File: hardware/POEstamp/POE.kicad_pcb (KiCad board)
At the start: 4 copper layers, 100 x 50 mm, 127 parts, among them J1 0813-1X1T-57-F, J2 SWD, J3 MCU Port B, J4 MCU Port C, P1 PoE-, P2 PoE+, P3 GND, P4 +5V, P5 +12V, P6 +3V3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

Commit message: Included BOM info on everything except transistors. Updated many footprints to IPC footprints. Also added a SOD-128 footprint.
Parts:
- removed 1PIN (x4): P***, Connect:1pin
- removed C1: 0.1uF, 100V, X7R, Capacitors_SMD:c_0805
- removed C10, C11: 10nF, Capacitors_SMD:c_0603
- removed C12, C31, C37: 1uF, Capacitors_SMD:c_0603
- removed C13: 33nF, Capacitors_SMD:c_0603
- removed C14, C15: 100uF, 6.3V, X5R, Capacitors_SMD:c_1206
- removed C16, C18: 10uF, Capacitors_SMD:c_1206
- removed C17, C22, C24, C25: 10uF, Capacitors_SMD:c_0805
- removed C19, C26, C27, C28, C29, C30, C32, C33, C34, C35, C36, C38, C39: 100nF, Capacitors_SMD:c_0603
- removed C2: 1uF, 100V, Capacitors_SMD:c_1206
- removed C20: 47nF, Capacitors_SMD:c_0805
- removed C21: 180nF, Capacitors_SMD:c_0805
- removed C23: 22uF, Capacitors_SMD:c_0805
- removed C3: 68pF, 200V, Capacitors_SMD:c_0603
- removed C4: 4.7uF, 10V, Capacitors_SMD:c_0805
- removed C5: 4.7uF, 100v, rfid:EEE-2AA4R7UP
- removed C6: 470pF, Capacitors_SMD:c_0603
- removed C7: 27nF, Capacitors_SMD:c_0805
- removed C8: 2.8nF, 250VAC, YCAP, rfid:kemet_C900
- removed C9: 220uF, 6.3v, rfid:EEE-FK0J221P
- removed D1: SMB540, SMD_Packages:DO-214-AA_SMB
- removed D10, D11: LED, LEDs:LED-0603
- removed D12: 5V LED, LEDs:LED-0603
- removed D13: 1N5189, rfid:SOD-123
- removed D14: 1N4148, rfid:SOD-123
- removed D15: MBRA340T3G, SMD_Packages:DO-214-AC_SMA
- removed D16: 12V LED, LEDs:LED-0603
- removed D17: 3V3 LED, LEDs:LED-0603
- removed D2: SMAJ58A, SMD_Packages:DO-214-AC_SMA
- removed D3, D4, D7: BAS516, rfid:SOD-523
- removed D5: 1N5237B, 8.2V, rfid:SOD-123
- removed D6, D9: CDNBS04-B08200, rfid:CDNBS04
- removed D8: TLV431, SMD_Packages:SOT-23
- removed G1: 25MHz OSC, rfid:Si501_2.5x2
- removed G2: 24MHz OSC, rfid:Si501_2.5x2
- removed J1: 0813-1X1T-57-F, rfid:0813-1X1T-57-F
- removed J2: SWD, rfid:JST_PH_5pin
- removed J3: MCU Port B, rfid:16_pin_breakout
- removed J4: MCU Port C, rfid:16_pin_breakout
- removed L1: 3.3uH, SMD_Packages:SMD-0805
- removed L2: choke, SMD_Packages:SMD-0805
- removed L3: 10uH, rfid:SRU1048
- removed L4: 15uH, rfid:NR6028
- removed P1: PoE-, Connect:PINTST
- removed P2: PoE+, Connect:PINTST
- removed P3: GND, Connect:PINTST
- removed P4: +5V, Connect:PINTST
- removed P5: +12V, Connect:PINTST
- removed P6: +3V3, Connect:PINTST
- removed P7: 12V_Switch, rfid:SIL2-3.5mm
- removed Q1: SI3440DV, NFET, rfid:TSOP-6
- removed Q2: MMBTA42, SMD_Packages:SOT-23_Inv2
- removed Q3: 2N7002, SMD_Packages:SOT-23-GDS
- removed Q4: MOSFET_N, SMD_Packages:SOT-23-GDS
- removed R1, R26, R29, R36: 10k, SMD_Packages:SMD-0603
- removed R10: 10R, SMD_Packages:SMD-0603
- removed R11, R17, R20: 1k, SMD_Packages:SMD-0603
- removed R12: 47k, SMD_Packages:SMD-0603
- removed R13: 100k, 1%, SMD_Packages:SMD-0603
- removed R14: 33.2k, SMD_Packages:SMD-0603
- removed R15, R16, R18, R19: 49R9, SMD_Packages:SMD-0603
- removed R2, R3: 220K, SMD_Packages:SMD-0603
- removed R21, R35: 470R, SMD_Packages:SMD-0603
- removed R22, R30: 2.8k, SMD_Packages:SMD-0603
- removed R23: 226k, SMD_Packages:SMD-0603
- removed R24: 1.4k, SMD_Packages:SMD-0805
- removed R25: 31.2k, SMD_Packages:SMD-0603
- removed R27: 143k, SMD_Packages:SMD-0603
- removed R28: 16.2k, SMD_Packages:SMD-0603
- removed R31: 2.32k, SMD_Packages:SMD-0603
- removed R32, R33: 24.9, SMD_Packages:SMD-0603
- removed R34: 4.7k, SMD_Packages:SMD-0603
- removed R4, R400: 0.250R, SMD_Packages:SMD-0805
- removed R5: 4.7K, SMD_Packages:SMD-0603
- removed R6: 510R, SMD_Packages:SMD-0603
- removed R7: 100R, 1/8W, SMD_Packages:SMD-0805
- removed R8: 100k, SMD_Packages:SMD-0603
- removed R9: 6.8k, SMD_Packages:SMD-0603
- removed SW1: reset, rfid:TE-Switch-FSM-JSM
- removed SYM: Symbol_OSHW-Logo_SilkScreen_07Jul2012, Symbols:Symbol_OSHW-Logo_SilkScreen
- removed T1: PA1134, rfid:PA1134
- removed U1: LTC4267-3, rfid:SSOP-16
- removed U2: ENC28J60, SMD_Packages:SSOP-28
- removed U3: PS2811, rfid:SSOP-4
- removed U4: MCP16301, SMD_Packages:SOT-23-6
- removed U5: TPS61175, rfid:HTSSOP-14-1EP
- removed U6: STM32F100RC, rfid:LQFP64
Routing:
- net 3V3: track 196.8 -> 0.00 mm, vias 11 -> 0
- net GND: track 172.3 -> 0.00 mm, vias 62 -> 0
- net 5VPoE: track 123.2 -> 0.00 mm, vias 16 -> 0
- net /EthernetINT: track 88.5 -> 0.00 mm, vias 2 -> 0
- net /EthernetSI: track 85.5 -> 0.00 mm, vias 2 -> 0
- net /EthernetSO: track 85.1 -> 0.00 mm, vias 2 -> 0
- net /EthernetSCK: track 84.6 -> 0.00 mm, vias 2 -> 0
- net /EthernetCS: track 84.3 -> 0.00 mm, vias 2 -> 0
- net GNDA: track 68.3 -> 0.00 mm, vias 14 -> 0
- net /nRST: track 54.5 -> 0.00 mm
- net /PVcc: track 42.1 -> 0.00 mm, vias 3 -> 0
- net /PB15: track 37.4 -> 0.00 mm, vias 1 -> 0
- net Net-(C2-Pad1): track 34.4 -> 0.00 mm, vias 1 -> 0
- net /PB10: track 34.4 -> 0.00 mm, vias 1 -> 0
- net /12VSwitch: track 33.1 -> 0.00 mm, vias 2 -> 0
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- removed copper zone on F.Cu, net 12V
- removed copper zone on In1.Cu, net 12V
- removed copper zone on B.Cu, net 3V3
- removed copper zone on F.Cu, net 3V3
- removed copper zone on B.Cu, net 5VPoE
- removed copper zone on F.Cu, net 5VPoE
- removed copper zone on B.Cu, net GND
- removed copper zone on F.Cu, net GND
- removed copper zone on In2.Cu, net GND
- removed copper zone on B.Cu, net GNDA
- removed copper zone on F.Cu, net GNDA
- removed copper zone on In2.Cu, net GNDA
- removed copper zone on F.Cu, net Net-(C19-Pad2)
- removed copper zone on F.Cu, net Net-(D1-Pad1)
- removed copper zone on F.Cu, net Net-(D15-Pad1)
- removed copper zone on B.Cu, net Net-(Q1-Pad1)
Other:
- board outline removed
- board text removed: "+"
- board text removed: "-"
- board text removed: "1"
- board text removed: "12V"
- board text removed: "2"
- board text removed: "3"
- board text removed: "3.3V"
- board text removed: "4"
- board text removed: "5V"
- board text removed: "Board Layers:"
- board text removed: "CERN OHL v1.2"
- board text removed: "GND"
- board text removed: "Jon Neal https://github.com/reportingsjr/rfidBoard Version 1"
- board text removed: "MCU Port B"
- board text removed: "MCU Port C"
- board text removed: "Pin 1"
- board text removed: "Reset"

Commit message: Initial netlist import and layer setup.
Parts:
- added C1: 0.1uF, 100V, X7R, IPC7351-Nominal:CAPC2012X95, F.Cu at (188.6, 111.5)
- added C10: 100nF, IPC7351-Nominal:CAPC1608X90, F.Cu at (191.1, 123.3)
- added C11: 100nF, IPC7351-Nominal:CAPC1608X90, F.Cu at (205.3, 110.6)
- added C12: 1uF, IPC7351-Nominal:CAPC1608X90, F.Cu at (206.4, 114.5)
- added C13: 33nF, IPC7351-Nominal:CAPC1608X95, F.Cu at (198.9, 121.8)
- added C14: 100uF, 6.3V, X5R, IPC7351-Nominal:CAPC3216X180, F.Cu at (194.9, 105.8)
- added C15: 100uF, 6.3V, X5R, IPC7351-Nominal:CAPC3216X180, F.Cu at (201.8, 96.3)
- added C16: 1uF, IPC7351-Nominal:CAPC1608X90, F.Cu at (213.6, 106.1)
- added C17: 1uF, IPC7351-Nominal:CAPC1608X90, F.Cu at (217.5, 103.6)
- added C2: 1uF, 100V, IPC7351-Nominal:CAPC3216X180, F.Cu at (217.3, 89.1)
- added C3: 68pF, 200V, IPC7351-Nominal:CAPC1608X87, F.Cu at (171.9, 123.6)
- added C4: 4.7uF, 10V, IPC7351-Nominal:CAPC2012X135, F.Cu at (217.5, 86.5)
- added C5: 4.7uF, 100v, rfid:EEE-2AA4R7UP, F.Cu at (174.5, 117.4)
- added C6: 470pF, IPC7351-Nominal:CAPC1608X90, F.Cu at (191.1, 121.3)
- added C7: 27nF, IPC7351-Nominal:CAPC2012X88, F.Cu at (209.9, 109.3)
- added C8: 2.8nF, 250VAC, YCAP, IPC7351-Nominal:CAPC4532X150, F.Cu at (189.7, 96.2)
- added C9: 220uF, 6.3v, rfid:EEE-FK0J221P, F.Cu at (151.8, 120.2)
- added D1: PMEG3050EP, rfid:SOD-128, F.Cu at (206.2, 101.8)
- added D12: 5V LED, LEDs:LED-0603, F.Cu at (214.1, 98.2)
- added D2: SMAJ58A, IPC7351-Nominal:DIOM5436X265, F.Cu at (164.4, 121.8)
- added D3: BAS516, rfid:SOD-523, F.Cu at (192.0, 115.3)
- added D4: BAS516, rfid:SOD-523, F.Cu at (200.2, 109.8)
- added D5: 1N5237B, 8.2V, rfid:SOD-123, F.Cu at (194.8, 101.5)
- added D6: CDNBS04-B08200, rfid:CDNBS04, F.Cu at (189.3, 88.3)
- added D7: BAS516, rfid:SOD-523, F.Cu at (217.1, 93.0)
- added D8: TLV431, smd-semi:SOT-23, F.Cu at (205.6, 107.7)
- added D9: CDNBS04-B08200, rfid:CDNBS04, F.Cu at (175.7, 104.3)
- added J1: 0813-1X1T-57-F, rfid:0813-1X1T-57-F, F.Cu at (152.5, 92.5)
- added L1: 3.3uH, IPC7351-Nominal:INDC2012X130, F.Cu at (209.9, 106.9)
- added P1: PoE-, Connect:PINTST, F.Cu at (202.4, 114.7)
- added P2: PoE+, Connect:PINTST, F.Cu at (213.5, 103.0)
- added P3: GND, Connect:PINTST, F.Cu at (195.4, 120.3)
- added P4: +5V, Connect:PINTST, F.Cu at (218.7, 98.0)
- added P5: CONN_01X05, conn-2mm:CONN-2MM-F-1x5, F.Cu at (214.8, 83.1)
- added P6: 5Vout, Connect:1pin, F.Cu at (211.5, 89.5)
- added P7: GNDout, Connect:1pin, F.Cu at (186.0, 116.9)
- added Q1: SI3440DV, NFET, rfid:TSOP-6, F.Cu at (202.2, 88.0)
- added Q2: 2N7002, smd-semi:SOT-23, F.Cu at (197.6, 114.4)
- added Q3: MMBTA42, smd-semi:SOT-23, F.Cu at (186.0, 122.5)
- added R1: 10k, IPC7351-Nominal:RESC1608X55, F.Cu at (221.0, 101.1)
- added R10: 10R, IPC7351-Nominal:RESC1608X55, F.Cu at (209.9, 111.5)
- added R11: 1k, IPC7351-Nominal:RESC1608X55, F.Cu at (206.4, 116.5)
- added R12: 47k, IPC7351-Nominal:RESC1608X55, F.Cu at (209.9, 114.5)
- added R13: 100k, 1%, IPC7351-Nominal:RESC1608X55, F.Cu at (178.6, 123.6)
- added R14: 33.2k, IPC7351-Nominal:RESC1608X55, F.Cu at (199.0, 117.9)
- added R2: 220K, IPC7351-Nominal:RESC1608X55, F.Cu at (194.9, 123.4)
- added R21: 470R, IPC7351-Nominal:RESC1608X55, F.Cu at (206.4, 112.6)
- added R22: 2.8k, IPC7351-Nominal:RESC1608X55, F.Cu at (217.0, 106.1)
- added R3: 220K, IPC7351-Nominal:RESC1608X55, F.Cu at (217.5, 101.6)
- added R4: 0.250R, IPC7351-Nominal:RESC2013X65, F.Cu at (211.4, 94.4)
- added R400: 0.250R, IPC7351-Nominal:RESC2013X65, F.Cu at (191.3, 119.1)
- added R5: 4.7K, IPC7351-Nominal:RESC1608X55, F.Cu at (202.4, 119.8)
- added R6: 510R, IPC7351-Nominal:RESC1608X55, F.Cu at (198.9, 119.8)
- added R7: 100R, 1/8W, IPC7351-Nominal:RESC2012X70, F.Cu at (193.2, 108.4)
- added R8: 100k, IPC7351-Nominal:RESC1608X55, F.Cu at (202.6, 117.9)
- added R9: 6.8k, IPC7351-Nominal:RESC1608X55, F.Cu at (213.5, 109.1)
- added T1: PA1134, rfid:PA1134, F.Cu at (171.8, 95.9)
- added U1: LTC4267-3, IPC7351-Nominal:SOP63P600X175-16, F.Cu at (164.3, 116.3)
- added U3: PS2811, rfid:SSOP-4, F.Cu at (186.0, 104.3)
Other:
- copper layers 4 -> 2

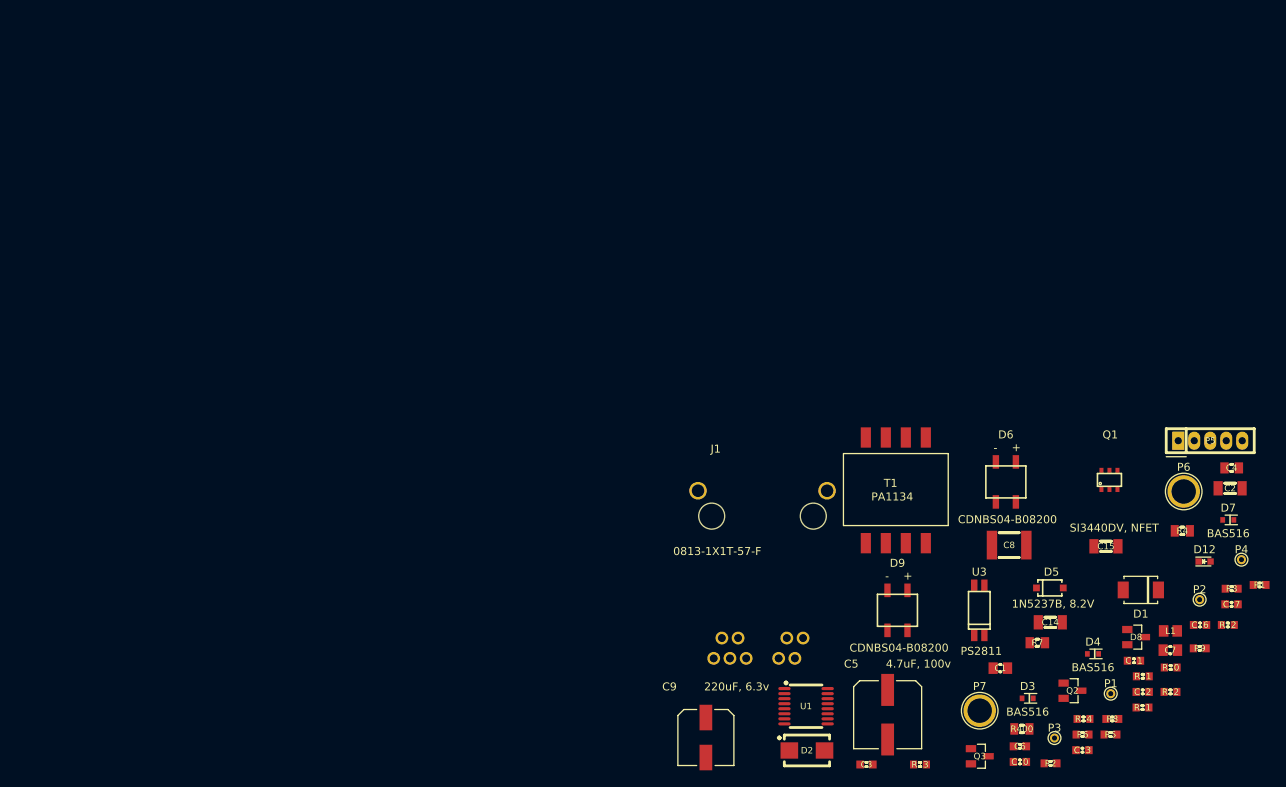
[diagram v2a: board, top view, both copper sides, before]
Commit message: Initial component arrangement.
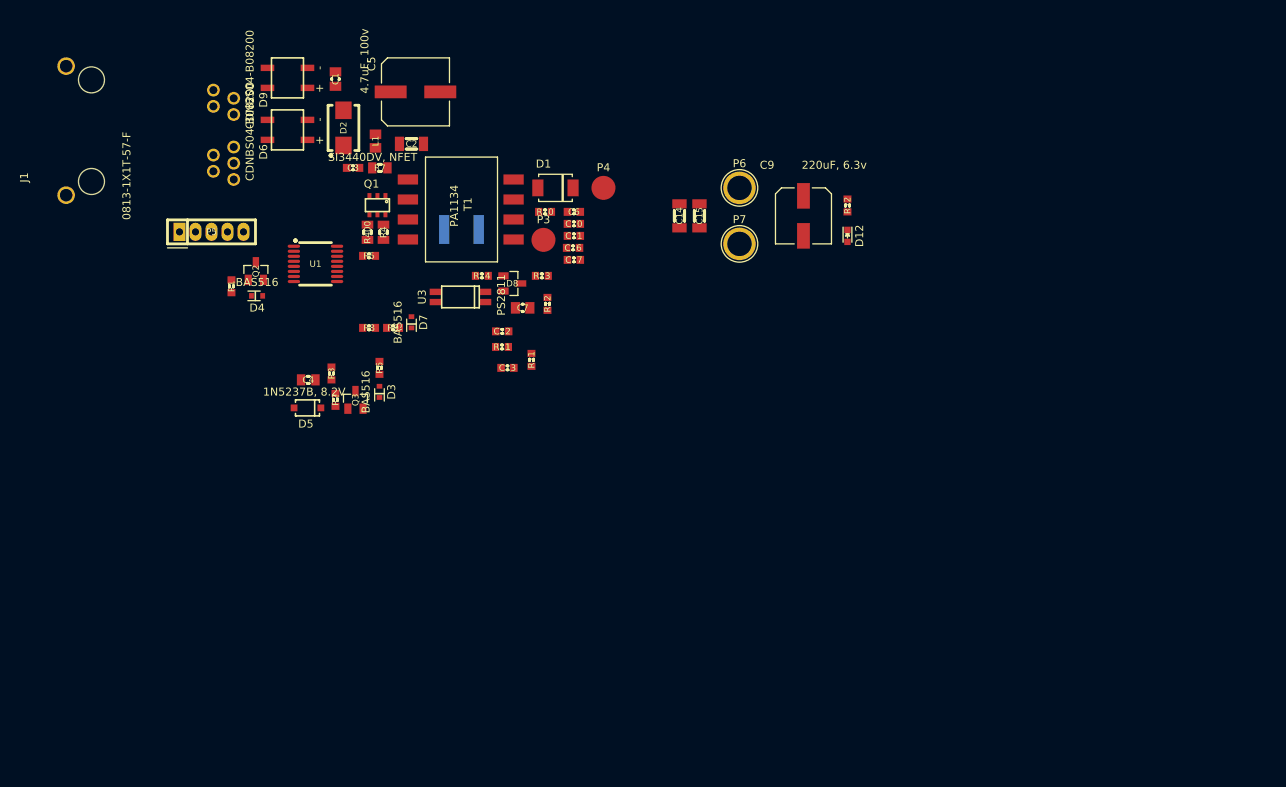
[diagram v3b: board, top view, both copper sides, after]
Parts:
- removed P1: PoE-, Connect:PINTST
- removed P2: PoE+, Connect:PINTST
- C8: moved to B.Cu
- P3, P4: footprint Connect:PINTST -> Measurement_Points:Measurement_Point_Round-SMD-Pad_Big
- moved R1 133.8 mm to (92.5, 63.8), turned to 90 degrees
- moved P5 127.5 mm to (90.0, 57.0)
- moved L1 116.7 mm to (110.5, 45.6), turned to 270 degrees
- moved C4 115.9 mm to (102.1, 75.5), turned to 180 degrees
- moved R3 115.7 mm to (105.0, 74.7), turned to 270 degrees
- moved Q2 114.8 mm to (95.5, 61.9), turned to 90 degrees
- moved D4 113.7 mm to (95.7, 65.0), turned to 180 degrees
- moved C1 111.0 mm to (105.5, 37.9), turned to 90 degrees
- moved C2 111.0 mm to (115.0, 46.0)
- moved R5 110.3 mm to (109.7, 60.0)
- moved R9 108.5 mm to (112.7, 69.0)
- moved R4 106.6 mm to (111.5, 57.0), turned to 270 degrees
- moved D7 105.0 mm to (115.0, 68.3), turned to 270 degrees
- moved R8 105.0 mm to (109.7, 69.0)
- moved R400 102.7 mm to (109.5, 57.0), turned to 270 degrees
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
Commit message: Adjusted design rules a bit for OSHPark
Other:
- rule via_min_size: 0.3 -> 0.6
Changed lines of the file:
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@@
     (via_size 0.6)
     (via_drill 0.3)
-    (via_min_size 0.3)
+    (via_min_size 0.6)
     (via_min_drill 0.3)
-    (user_via 0.45 0.3)
-    (user_via 0.5 0.35)
+    (user_via 0.6 0.3)
+    (user_via 0.8 0.5)
     (uvia_size 0.508)
     (uvia_drill 0.127)

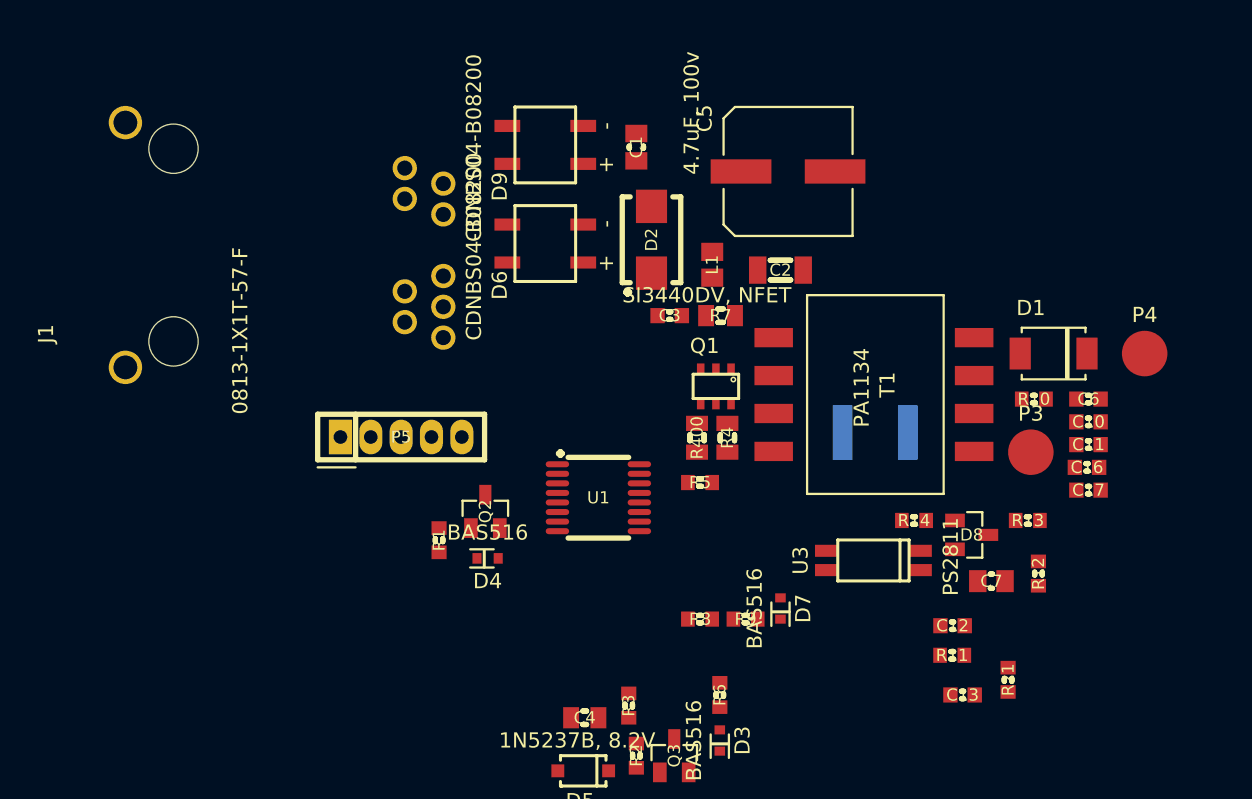
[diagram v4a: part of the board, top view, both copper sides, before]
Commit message: Added board outline and 3.5mm mounting holes on a 60mmx30mm grid.
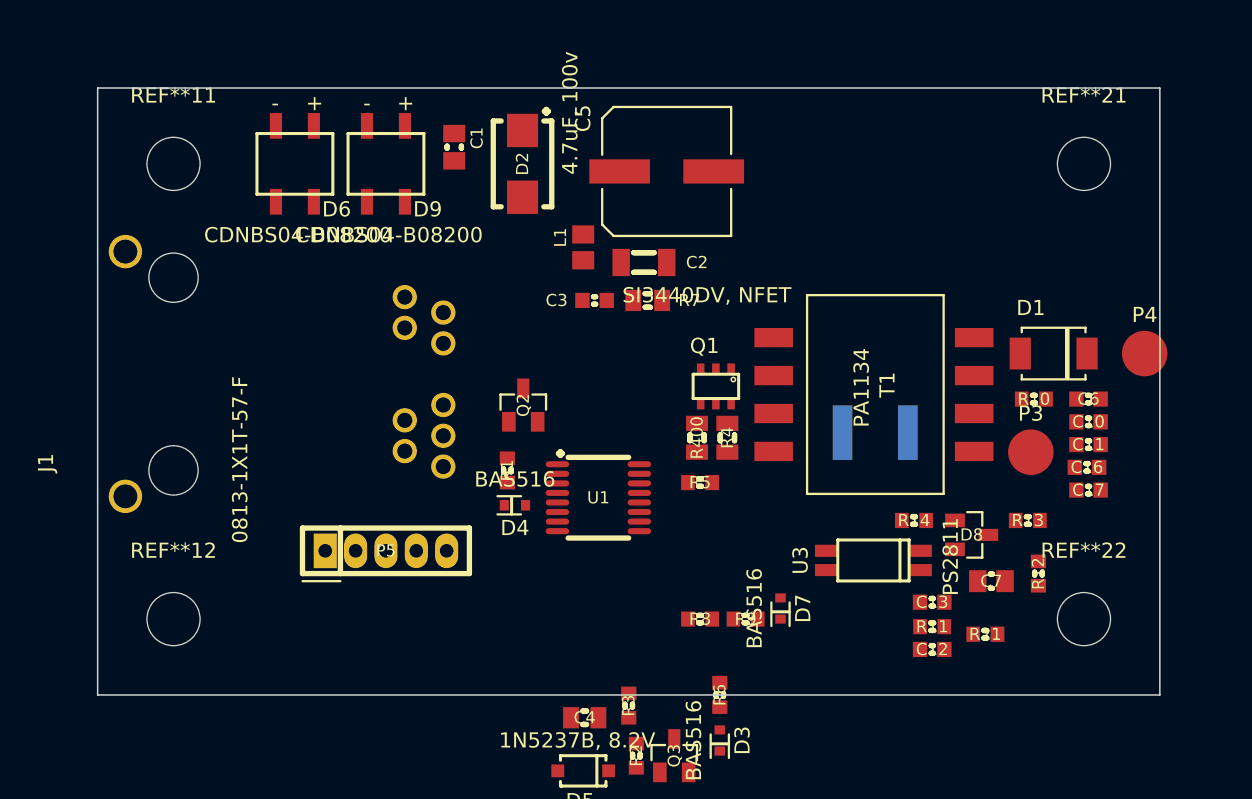
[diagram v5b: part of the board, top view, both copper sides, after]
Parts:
- added REF**11: MountingHole_3-5mm, Mounting_Holes:MountingHole_3-5mm, F.Cu at (75.0, 39.0)
- added REF**12: MountingHole_3-5mm, Mounting_Holes:MountingHole_3-5mm, F.Cu at (75.0, 69.0)
- added REF**21: MountingHole_3-5mm, Mounting_Holes:MountingHole_3-5mm, F.Cu at (135.0, 39.0)
- added REF**22: MountingHole_3-5mm, Mounting_Holes:MountingHole_3-5mm, F.Cu at (135.0, 69.0)
- moved D6 17.3 mm to (83.0, 39.0), turned to 0 degrees
- moved C1 12.0 mm to (93.5, 37.9), turned to 270 degrees
- moved D9 10.6 mm to (89.0, 39.0), turned to 0 degrees
- moved D2 9.86 mm to (98.0, 39.0), turned to 270 degrees
- moved C2 9.01 mm to (106.0, 45.5)
- moved L1 8.58 mm to (102.0, 44.5)
- moved J1 8.50 mm to (75.0, 59.2)
- moved C5 8.00 mm to (107.5, 39.5)
- moved P5 7.57 mm to (89.0, 64.5)
- moved Q2 7.43 mm to (98.0, 54.9)
- moved R1 6.44 mm to (97.0, 59.2)
- moved C13 6.43 mm to (125.0, 67.9), turned to 180 degrees
- moved C3 5.05 mm to (102.8, 48.0)
- moved R7 4.90 mm to (106.2, 48.0)
- moved D4 3.94 mm to (97.5, 61.5)
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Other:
- board outline added: 70 x 40 mm

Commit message: Almost everything is in an OK spot on the PCB.
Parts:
- moved C9 40.0 mm to (125.8, 43.2), turned to 270 degrees
- moved P7 39.4 mm to (123.0, 37.0)
- moved P6 30.9 mm to (128.8, 37.0)
- moved R2 28.2 mm to (98.2, 50.8)
- moved Q3 27.3 mm to (101.2, 51.5)
- moved D3 25.0 mm to (106.0, 52.5)
- moved D5 24.5 mm to (98.2, 54.8), turned to 270 degrees
- moved R6 24.1 mm to (106.8, 50.2), turned to 0 degrees
- moved C4 23.6 mm to (104.2, 52.0), turned to 90 degrees
- moved Q2 16.5 mm to (110.2, 66.0), turned to 270 degrees
- moved R3 15.8 mm to (99.8, 59.8), turned to 90 degrees
- moved R1 9.76 mm to (104.0, 66.0), turned to 0 degrees
- moved D4 9.52 mm to (106.2, 65.2), turned to 270 degrees
- moved R8 5.75 mm to (104.0, 68.2)
- moved R9 5.21 mm to (107.5, 68.8)
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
